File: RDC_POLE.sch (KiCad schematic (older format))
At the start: 32 parts, among them J1 CN_ARM, Q1 BC807, Q2 BC807, U2 AD8397ARZ, X1 8.192MHz

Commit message: agregado el segundo RDC, leds conectados a +5v, asignados footprints
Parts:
- removed C13: 100n, Capacitor_SMD:C_1206_3216Metric_Pad1.42x1.75mm_HandSolder, symbol Device:CP1
- removed R7: 10K, Resistor_SMD:R_1206_3216Metric_Pad1.42x1.75mm_HandSolder, symbol Device:R
- J1: value CN_ARM -> CN_POLE
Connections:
- net labels added: GPIO3
- net labels removed: GPIO2
- wire segments 129 -> 124

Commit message: cambios en el placement
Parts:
- renumbered AD1 to AD2, C11 to C14, C12 to C15, C14 to C16, C3 to C17, C6 to C18, C4 to C19, C7 to C20, C5 to C21, C8 to C22, C15 to C23, C9 to C24, C10 to C25, D1 to D3, D2 to D4, J1 to J2, Q1 to Q3, Q2 to Q4, R4 to R13, R6 to R14, R8 to R15, R9 to R16, R3 to R17, R1 to R18, R10 to R19, R11 to R20, R13 to R21, X1 to X2

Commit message: routeado completo, quedan 32 vias
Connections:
- wire segments 124 -> 126
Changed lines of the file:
@@
 Wire Wire Line
 	7900 4250 7600 4250
-Text Label 10400 4350 2    60   ~ 0
-COS
-Text Label 10400 4450 2    60   ~ 0
-COSLO
-Text Label 10400 4150 2    60   ~ 0
-SINLO
-Text Label 10400 4050 2    60   ~ 0
-SIN
-Wire Wire Line
-	10500 4450 10100 4450
-Wire Wire Line
-	10500 4350 10100 4350
-Wire Wire Line
-	10500 4150 10100 4150
-Wire Wire Line
-	10500 4050 10100 4050
-Text Label 10400 4550 2    60   ~ 0
+Text Label 10500 4050 2    60   ~ 0
 AGND
-Text Label 10400 4250 2    60   ~ 0
+Text Label 10500 3750 2    60   ~ 0
 AGND
-Text Label 10400 3950 2    60   ~ 0
+Text Label 10500 3450 2    60   ~ 0
 AGND
-Wire Wire Line
-	10500 4550 10100 4550
-Wire Wire Line
-	10500 4250 10100 4250
-Wire Wire Line
-	10500 3950 10100 3950
-Wire Wire Line
-	9950 3850 10500 3850
-Wire Wire Line
-	9950 3750 10500 3750
-$Comp
-L Connector:Screw_Terminal_01x09 J?
-U 1 1 5F08F1F4
-P 10700 4150
-AR Path="/5F08F1F4" Ref="J?"  Part="1"
-AR Path="/5EF45E27/5F08F1F4" Ref="J?"  Part="1"
-AR Path="/5F077C82/5F08F1F4" Ref="J2"  Part="1"
-F 0 "J2" H 10780 4192 50  0000 L CNN
-F 1 "CN_POLE" H 10780 4101 50  0000 L CNN
-F 2 "TerminalBlock_Phoenix:TerminalBlock_Phoenix_MKDS-1,5-9-5.08_1x09_P5.08mm_Horizontal" H 10700 4150 50  0001 C CNN
-F 3 "~" H 10700 4150 50  0001 C CNN
-	1    10700 4150
-	1    0    0    -1
-$EndComp
 $Comp
 L power:+12V #PWR?
@@
 	8300 4250 8300 5450
 Wire Wire Line
-	9950 3850 9950 5100
-Wire Wire Line
 	9500 5100 9300 5100
 Wire Wire Line
@@
 Wire Wire Line
 	9950 5100 9950 5450
-Wire Wire Line
-	9950 2950 9950 3300
 Wire Wire Line
 	9300 3300 9500 3300
@@
 Wire Wire Line
 	5800 2900 5800 2950
+Text Label 10500 3550 2    60   ~ 0
+SIN
+Text Label 10500 3650 2    60   ~ 0
+SINLO
+Wire Wire Line
+	9950 2950 9950 3300
+Text Label 10500 3250 2    60   ~ 0
+COS
+Text Label 10500 3350 2    60   ~ 0
+COSLO
+Wire Wire Line
+	9950 3850 9950 5100
+Wire Wire Line
+	10600 3250 10200 3250
+Wire Wire Line
+	10600 3350 10200 3350
+$Comp
+L Connector:Screw_Terminal_01x09 J?
+U 1 1 5F08F1F4
+P 10800 3650
+AR Path="/5F08F1F4" Ref="J?"  Part="1"
+AR Path="/5EF45E27/5F08F1F4" Ref="J?"  Part="1"
+AR Path="/5F077C82/5F08F1F4" Ref="J2"  Part="1"
+F 0 "J2" H 10880 3692 50  0000 L CNN
+F 1 "CN_POLE" H 10880 3601 50  0000 L CNN
+F 2 "TerminalBlock_Phoenix:TerminalBlock_Phoenix_MKDS-1,5-9-5.08_1x09_P5.08mm_Horizontal" H 10800 3650 50  0001 C CNN
+F 3 "~" H 10800 3650 50  0001 C CNN
+	1    10800 3650
+	1    0    0    -1
+$EndComp
+Wire Wire Line
+	10600 3450 10200 3450
+Wire Wire Line
+	10600 3750 10200 3750
+Wire Wire Line
+	10600 4050 10200 4050
+Wire Wire Line
+	10600 3550 10200 3550
+Wire Wire Line
+	10600 3650 10200 3650
+Wire Wire Line
+	10050 3950 10600 3950
+Wire Wire Line
+	9950 3850 10600 3850
+Connection ~ 9950 3850
+Wire Wire Line
+	9950 3750 10050 3750
+Wire Wire Line
+	10050 3750 10050 3950
+Connection ~ 9950 3750
 $EndSCHEMATC

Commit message: cambiados conectores, agregado conversor 3,3->TTL drivers
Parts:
- removed J2: CN_POLE, TerminalBlock_Phoenix:TerminalBlock_Phoenix_MKDS-1,5-9-5.08_1x09_P5.08mm_Horizontal, symbol Connector:Screw_Terminal_01x09
- added J4: COS, Connector_JST:JST_EH_S3B-EH_1x03_P2.50mm_Horizontal, symbol Connector_Generic:Conn_01x03
- added J5: SIN, Connector_JST:JST_EH_S3B-EH_1x03_P2.50mm_Horizontal, symbol Connector_Generic:Conn_01x03
- added J6: EXC, Connector_JST:JST_EH_S3B-EH_1x03_P2.50mm_Horizontal, symbol Connector_Generic:Conn_01x03
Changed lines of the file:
@@
 $Descr A4 11693 8268
 encoding utf-8
-Sheet 4 5
+Sheet 4 6
 Title ""
 Date ""
@@
 Text Label 10500 4050 2    60   ~ 0
 AGND
-Text Label 10500 3750 2    60   ~ 0
+Text Label 10500 3600 2    60   ~ 0
 AGND
-Text Label 10500 3450 2    60   ~ 0
+Text Label 10500 3150 2    60   ~ 0
 AGND
 $Comp
@@
 Wire Wire Line
 	5800 2900 5800 2950
-Text Label 10500 3550 2    60   ~ 0
+Text Label 10500 3400 2    60   ~ 0
 SIN
-Text Label 10500 3650 2    60   ~ 0
+Text Label 10500 3500 2    60   ~ 0
 SINLO
 Wire Wire Line
 	9950 2950 9950 3300
-Text Label 10500 3250 2    60   ~ 0
+Text Label 10500 2950 2    60   ~ 0
 COS
-Text Label 10500 3350 2    60   ~ 0
+Text Label 10500 3050 2    60   ~ 0
 COSLO
 Wire Wire Line
 	9950 3850 9950 5100
 Wire Wire Line
-	10600 3250 10200 3250
-Wire Wire Line
-	10600 3350 10200 3350
-$Comp
-L Connector:Screw_Terminal_01x09 J?
-U 1 1 5F08F1F4
-P 10800 3650
-AR Path="/5F08F1F4" Ref="J?"  Part="1"
-AR Path="/5EF45E27/5F08F1F4" Ref="J?"  Part="1"
-AR Path="/5F077C82/5F08F1F4" Ref="J2"  Part="1"
-F 0 "J2" H 10880 3692 50  0000 L CNN
-F 1 "CN_POLE" H 10880 3601 50  0000 L CNN
-F 2 "TerminalBlock_Phoenix:TerminalBlock_Phoenix_MKDS-1,5-9-5.08_1x09_P5.08mm_Horizontal" H 10800 3650 50  0001 C CNN
-F 3 "~" H 10800 3650 50  0001 C CNN
-	1    10800 3650
-	1    0    0    -1
-$EndComp
-Wire Wire Line
-	10600 3450 10200 3450
-Wire Wire Line
-	10600 3750 10200 3750
+	10600 2950 10200 2950
+Wire Wire Line
+	10600 3050 10200 3050
+Wire Wire Line
+	10600 3150 10200 3150
+Wire Wire Line
+	10600 3600 10200 3600
 Wire Wire Line
 	10600 4050 10200 4050
 Wire Wire Line
-	10600 3550 10200 3550
-Wire Wire Line
-	10600 3650 10200 3650
+	10600 3400 10200 3400
+Wire Wire Line
+	10600 3500 10200 3500
 Wire Wire Line
 	10050 3950 10600 3950
@@
 	10050 3750 10050 3950
 Connection ~ 9950 3750
+$Comp
+L Connector_Generic:Conn_01x03 J4
+U 1 1 5F0C4501
+P 10800 3050
+F 0 "J4" H 10880 3092 50  0000 L CNN
+F 1 "COS" H 10880 3001 50  0000 L CNN
+F 2 "Connector_JST:JST_EH_S3B-EH_1x03_P2.50mm_Horizontal" H 10800 3050 50  0001 C CNN
+F 3 "~" H 10800 3050 50  0001 C CNN
+	1    10800 3050
+	1    0    0    -1
+$EndComp
+$Comp
+L Connector_Generic:Conn_01x03 J5
+U 1 1 5F0C48DE
+P 10800 3500
+F 0 "J5" H 10880 3542 50  0000 L CNN
+F 1 "SIN" H 10880 3451 50  0000 L CNN
+F 2 "Connector_JST:JST_EH_S3B-EH_1x03_P2.50mm_Horizontal" H 10800 3500 50  0001 C CNN
+F 3 "~" H 10800 3500 50  0001 C CNN
+	1    10800 3500
+	1    0    0    -1
+$EndComp
+$Comp
+L Connector_Generic:Conn_01x03 J6
+U 1 1 5F0C52DE
+P 10800 3950
+F 0 "J6" H 10880 3992 50  0000 L CNN
+F 1 "EXC" H 10880 3901 50  0000 L CNN
+F 2 "Connector_JST:JST_EH_S3B-EH_1x03_P2.50mm_Horizontal" H 10800 3950 50  0001 C CNN
+F 3 "~" H 10800 3950 50  0001 C CNN
+	1    10800 3950
+	1    0    0    -1
+$EndComp
 $EndSCHEMATC

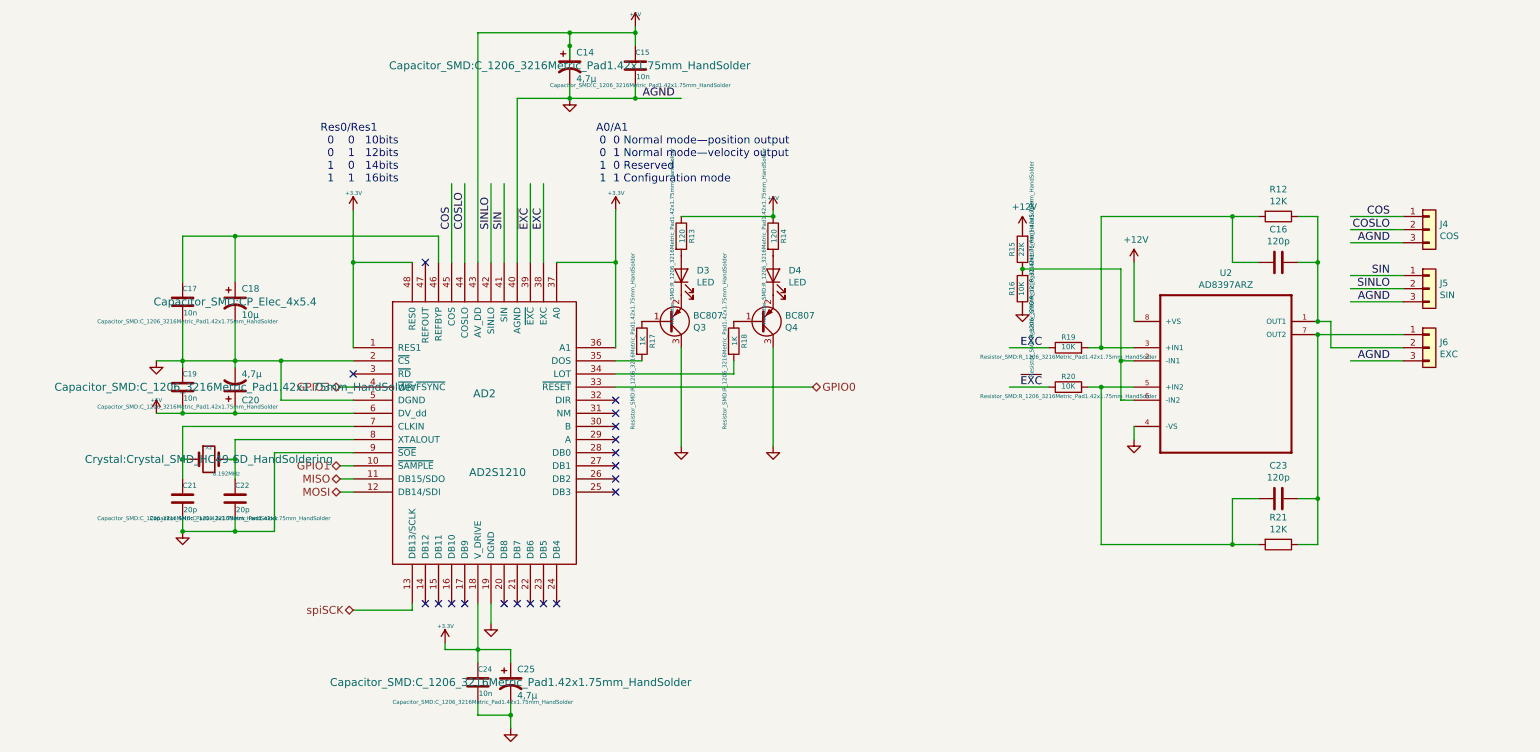
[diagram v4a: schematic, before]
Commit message: cambiado a conectores MOLEX KK, agregados test points para señales analogicas
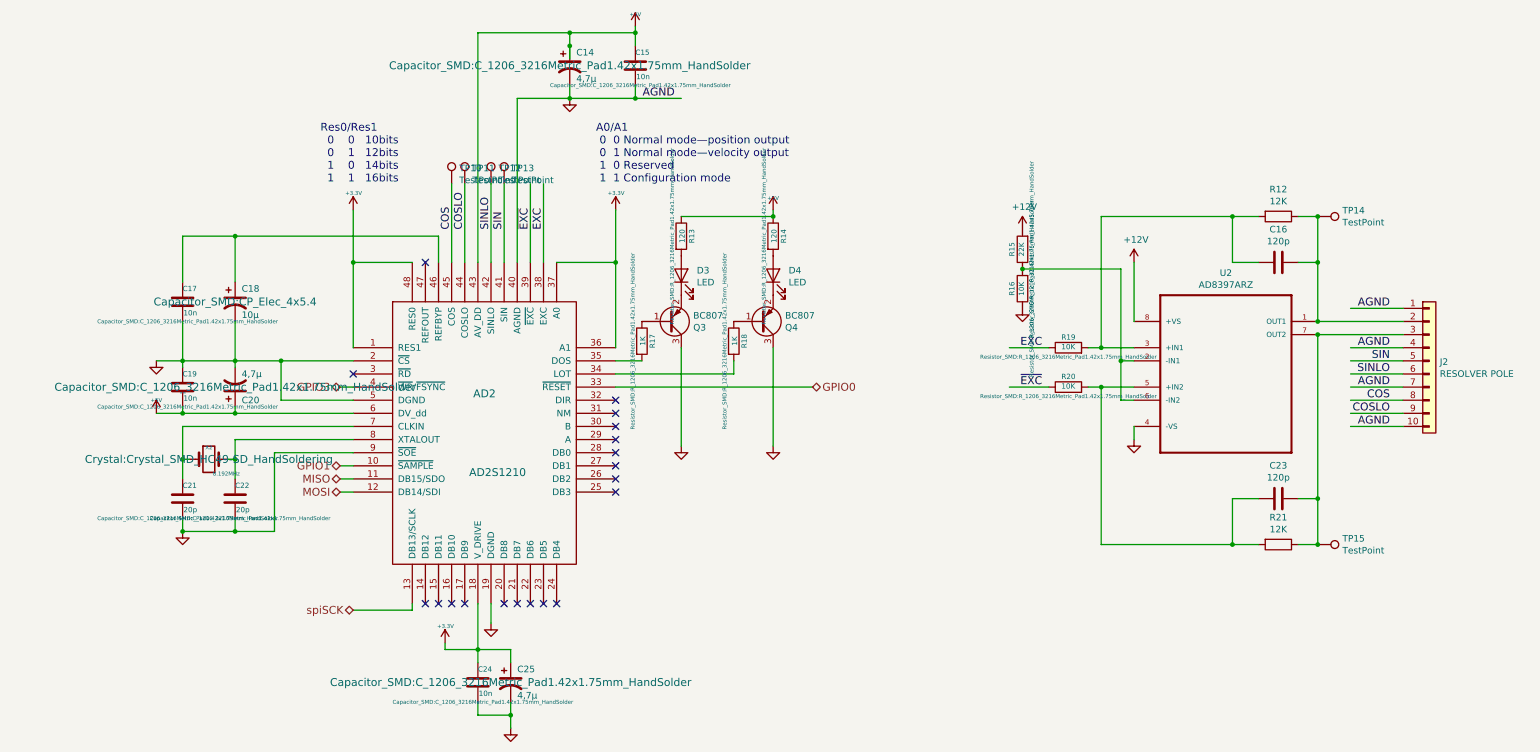
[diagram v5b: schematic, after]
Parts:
- removed J4: COS, Connector_JST:JST_EH_S3B-EH_1x03_P2.50mm_Horizontal, symbol Connector_Generic:Conn_01x03
- removed J5: SIN, Connector_JST:JST_EH_S3B-EH_1x03_P2.50mm_Horizontal, symbol Connector_Generic:Conn_01x03
- removed J6: EXC, Connector_JST:JST_EH_S3B-EH_1x03_P2.50mm_Horizontal, symbol Connector_Generic:Conn_01x03
- added J2: RESOLVER POLE, Connector_Molex:Molex_KK-254_AE-6410-10A_1x10_P2.54mm_Vertical, symbol Connector_Generic:Conn_01x10
- added TP10, TP11, TP12, TP13, TP14, TP15: TestPoint, TestPoint:TestPoint_THTPad_1.0x1.0mm_Drill0.5mm, symbol Connector:TestPoint
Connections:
- wire segments 126 -> 125
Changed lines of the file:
@@
 Wire Wire Line
 	7900 4250 7600 4250
-Text Label 10500 4050 2    60   ~ 0
+Text Label 10500 4550 2    60   ~ 0
 AGND
-Text Label 10500 3600 2    60   ~ 0
-AGND
-Text Label 10500 3150 2    60   ~ 0
+Text Label 10500 3950 2    60   ~ 0
 AGND
 $Comp
@@
 Wire Wire Line
 	5800 2900 5800 2950
-Text Label 10500 3400 2    60   ~ 0
-SIN
-Text Label 10500 3500 2    60   ~ 0
-SINLO
 Wire Wire Line
 	9950 2950 9950 3300
-Text Label 10500 2950 2    60   ~ 0
+Text Label 10500 4350 2    60   ~ 0
 COS
-Text Label 10500 3050 2    60   ~ 0
+Text Label 10500 4450 2    60   ~ 0
 COSLO
 Wire Wire Line
+	10600 4350 10200 4350
+Wire Wire Line
+	10600 4450 10200 4450
+Wire Wire Line
+	10600 3950 10200 3950
+Wire Wire Line
+	10600 4550 10200 4550
+Connection ~ 9950 3750
+$Comp
+L Connector_Generic:Conn_01x10 J2
+U 1 1 5F092EDC
+P 10800 4050
+F 0 "J2" H 10880 4042 50  0000 L CNN
+F 1 "RESOLVER POLE" H 10880 3951 50  0000 L CNN
+F 2 "Connector_Molex:Molex_KK-254_AE-6410-10A_1x10_P2.54mm_Vertical" H 10800 4050 50  0001 C CNN
+F 3 "~" H 10800 4050 50  0001 C CNN
+	1    10800 4050
+	1    0    0    -1
+$EndComp
+Text Label 10500 3650 2    60   ~ 0
+AGND
+Wire Wire Line
+	10600 3650 10200 3650
+$Comp
+L Connector:TestPoint TP14
+U 1 1 5F0B4618
+P 9950 2950
+F 0 "TP14" V 9904 3138 50  0000 L CNN
+F 1 "TestPoint" V 9995 3138 50  0000 L CNN
+F 2 "TestPoint:TestPoint_THTPad_1.0x1.0mm_Drill0.5mm" H 10150 2950 50  0001 C CNN
+F 3 "~" H 10150 2950 50  0001 C CNN
+	1    9950 2950
+	0    1    1    0
+$EndComp
+Connection ~ 9950 2950
+$Comp
+L Connector:TestPoint TP15
+U 1 1 5F0B53CC
+P 9950 5450
+F 0 "TP15" V 9904 5638 50  0000 L CNN
+F 1 "TestPoint" V 9995 5638 50  0000 L CNN
+F 2 "TestPoint:TestPoint_THTPad_1.0x1.0mm_Drill0.5mm" H 10150 5450 50  0001 C CNN
+F 3 "~" H 10150 5450 50  0001 C CNN
+	1    9950 5450
+	0    1    1    0
+$EndComp
+Connection ~ 9950 5450
+$Comp
+L Connector:TestPoint TP10
+U 1 1 5F0B5F68
+P 3350 2700
+F 0 "TP10" H 3408 2818 50  0000 L CNN
+F 1 "TestPoint" H 3408 2727 50  0000 L CNN
+F 2 "TestPoint:TestPoint_THTPad_1.0x1.0mm_Drill0.5mm" H 3550 2700 50  0001 C CNN
+F 3 "~" H 3550 2700 50  0001 C CNN
+	1    3350 2700
+	1    0    0    -1
+$EndComp
+$Comp
+L Connector:TestPoint TP11
+U 1 1 5F0B648D
+P 3450 2700
+F 0 "TP11" H 3508 2818 50  0000 L CNN
+F 1 "TestPoint" H 3508 2727 50  0000 L CNN
+F 2 "TestPoint:TestPoint_THTPad_1.0x1.0mm_Drill0.5mm" H 3650 2700 50  0001 C CNN
+F 3 "~" H 3650 2700 50  0001 C CNN
+	1    3450 2700
+	1    0    0    -1
+$EndComp
+$Comp
+L Connector:TestPoint TP12
+U 1 1 5F0B6AB2
+P 3650 2700
+F 0 "TP12" H 3708 2818 50  0000 L CNN
+F 1 "TestPoint" H 3708 2727 50  0000 L CNN
+F 2 "TestPoint:TestPoint_THTPad_1.0x1.0mm_Drill0.5mm" H 3850 2700 50  0001 C CNN
+F 3 "~" H 3850 2700 50  0001 C CNN
+	1    3650 2700
+	1    0    0    -1
+$EndComp
+$Comp
+L Connector:TestPoint TP13
+U 1 1 5F0B6E5F
+P 3750 2700
+F 0 "TP13" H 3808 2818 50  0000 L CNN
+F 1 "TestPoint" H 3808 2727 50  0000 L CNN
+F 2 "TestPoint:TestPoint_THTPad_1.0x1.0mm_Drill0.5mm" H 3950 2700 50  0001 C CNN
+F 3 "~" H 3950 2700 50  0001 C CNN
+	1    3750 2700
+	1    0    0    -1
+$EndComp
+Wire Wire Line
 	9950 3850 9950 5100
 Wire Wire Line
-	10600 2950 10200 2950
-Wire Wire Line
-	10600 3050 10200 3050
-Wire Wire Line
-	10600 3150 10200 3150
-Wire Wire Line
-	10600 3600 10200 3600
-Wire Wire Line
-	10600 4050 10200 4050
-Wire Wire Line
-	10600 3400 10200 3400
-Wire Wire Line
-	10600 3500 10200 3500
-Wire Wire Line
-	10050 3950 10600 3950
+	9950 3750 10600 3750
 Wire Wire Line
 	9950 3850 10600 3850
 Connection ~ 9950 3850
 Wire Wire Line
-	9950 3750 10050 3750
-Wire Wire Line
-	10050 3750 10050 3950
-Connection ~ 9950 3750
-$Comp
-L Connector_Generic:Conn_01x03 J4
-U 1 1 5F0C4501
-P 10800 3050
-F 0 "J4" H 10880 3092 50  0000 L CNN
-F 1 "COS" H 10880 3001 50  0000 L CNN
-F 2 "Connector_JST:JST_EH_S3B-EH_1x03_P2.50mm_Horizontal" H 10800 3050 50  0001 C CNN
-F 3 "~" H 10800 3050 50  0001 C CNN
-	1    10800 3050
-	1    0    0    -1
-$EndComp
-$Comp
-L Connector_Generic:Conn_01x03 J5
-U 1 1 5F0C48DE
-P 10800 3500
-F 0 "J5" H 10880 3542 50  0000 L CNN
-F 1 "SIN" H 10880 3451 50  0000 L CNN
-F 2 "Connector_JST:JST_EH_S3B-EH_1x03_P2.50mm_Horizontal" H 10800 3500 50  0001 C CNN
-F 3 "~" H 10800 3500 50  0001 C CNN
-	1    10800 3500
-	1    0    0    -1
-$EndComp
-$Comp
-L Connector_Generic:Conn_01x03 J6
-U 1 1 5F0C52DE
-P 10800 3950
-F 0 "J6" H 10880 3992 50  0000 L CNN
-F 1 "EXC" H 10880 3901 50  0000 L CNN
-F 2 "Connector_JST:JST_EH_S3B-EH_1x03_P2.50mm_Horizontal" H 10800 3950 50  0001 C CNN
-F 3 "~" H 10800 3950 50  0001 C CNN
-	1    10800 3950
-	1    0    0    -1
-$EndComp
+	10600 4150 10200 4150
+Wire Wire Line
+	10600 4050 10200 4050
+Wire Wire Line
+	10600 4250 10200 4250
+Text Label 10500 4150 2    60   ~ 0
+SINLO
+Text Label 10500 4050 2    60   ~ 0
+SIN
+Text Label 10500 4250 2    60   ~ 0
+AGND
 $EndSCHEMATC

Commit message: outline reducido, para revision por peers
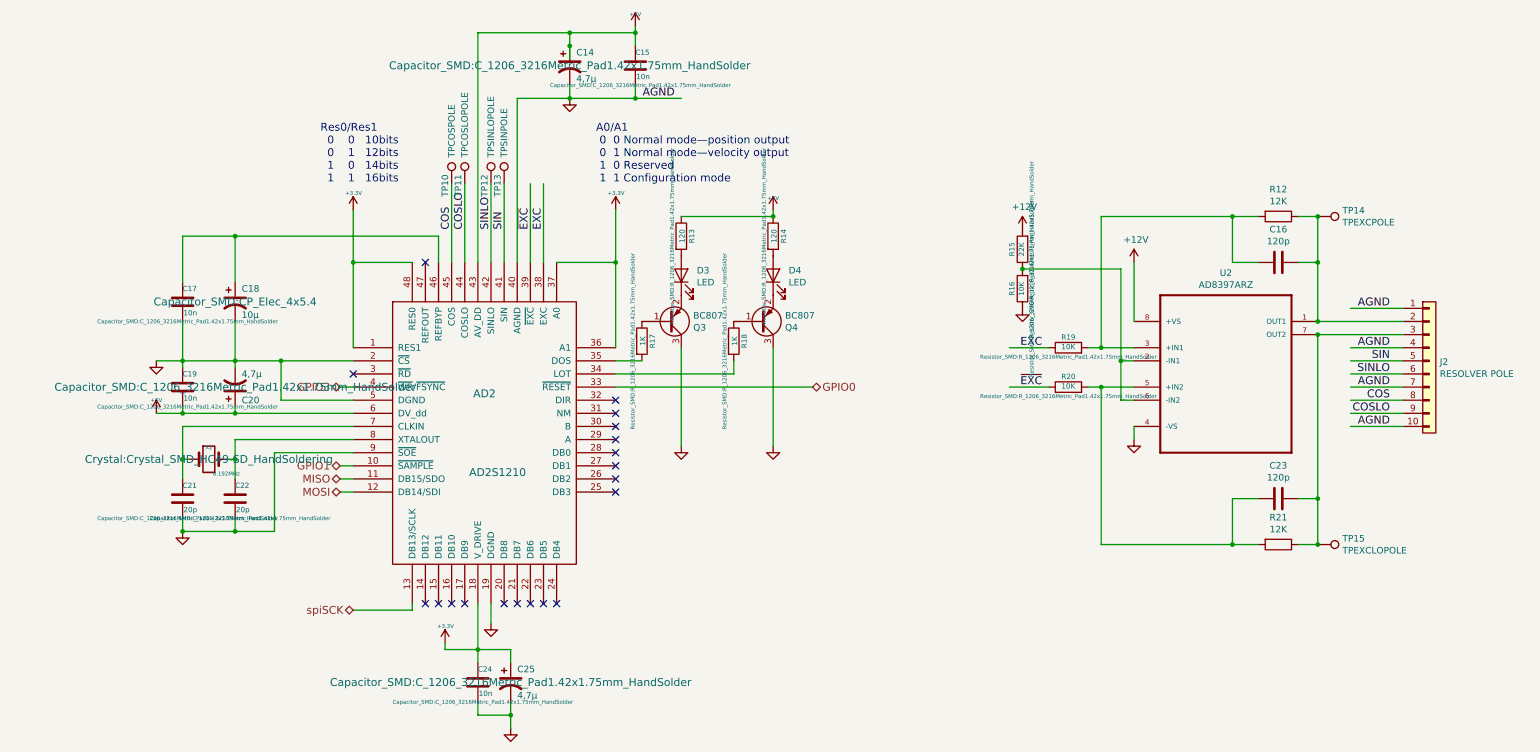
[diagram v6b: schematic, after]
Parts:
- TP10: value TestPoint -> TPCOSPOLE
- TP11: value TestPoint -> TPCOSLOPOLE
- TP12: value TestPoint -> TPSINLOPOLE
- TP13: value TestPoint -> TPSINPOLE
- TP14: value TestPoint -> TPEXCPOLE
- TP15: value TestPoint -> TPEXCLOPOLE
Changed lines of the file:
@@
 P 9950 2950
 F 0 "TP14" V 9904 3138 50  0000 L CNN
-F 1 "TestPoint" V 9995 3138 50  0000 L CNN
+F 1 "TPEXCPOLE" V 9995 3138 50  0000 L CNN
 F 2 "TestPoint:TestPoint_THTPad_1.0x1.0mm_Drill0.5mm" H 10150 2950 50  0001 C CNN
 F 3 "~" H 10150 2950 50  0001 C CNN
@@
 P 9950 5450
 F 0 "TP15" V 9904 5638 50  0000 L CNN
-F 1 "TestPoint" V 9995 5638 50  0000 L CNN
+F 1 "TPEXCLOPOLE" V 9995 5638 50  0000 L CNN
 F 2 "TestPoint:TestPoint_THTPad_1.0x1.0mm_Drill0.5mm" H 10150 5450 50  0001 C CNN
 F 3 "~" H 10150 5450 50  0001 C CNN
@@
 U 1 1 5F0B5F68
 P 3350 2700
-F 0 "TP10" H 3408 2818 50  0000 L CNN
-F 1 "TestPoint" H 3408 2727 50  0000 L CNN
+F 0 "TP10" V 3300 2600 50  0000 L CNN
+F 1 "TPCOSPOLE" V 3350 2900 50  0000 L CNN
 F 2 "TestPoint:TestPoint_THTPad_1.0x1.0mm_Drill0.5mm" H 3550 2700 50  0001 C CNN
 F 3 "~" H 3550 2700 50  0001 C CNN
@@
 U 1 1 5F0B648D
 P 3450 2700
-F 0 "TP11" H 3508 2818 50  0000 L CNN
-F 1 "TestPoint" H 3508 2727 50  0000 L CNN
+F 0 "TP11" V 3400 2600 50  0000 L CNN
+F 1 "TPCOSLOPOLE" V 3450 2900 50  0000 L CNN
 F 2 "TestPoint:TestPoint_THTPad_1.0x1.0mm_Drill0.5mm" H 3650 2700 50  0001 C CNN
 F 3 "~" H 3650 2700 50  0001 C CNN
@@
 U 1 1 5F0B6AB2
 P 3650 2700
-F 0 "TP12" H 3708 2818 50  0000 L CNN
-F 1 "TestPoint" H 3708 2727 50  0000 L CNN
+F 0 "TP12" V 3600 2600 50  0000 L CNN
+F 1 "TPSINLOPOLE" V 3650 2900 50  0000 L CNN
 F 2 "TestPoint:TestPoint_THTPad_1.0x1.0mm_Drill0.5mm" H 3850 2700 50  0001 C CNN
 F 3 "~" H 3850 2700 50  0001 C CNN
@@
 U 1 1 5F0B6E5F
 P 3750 2700
-F 0 "TP13" H 3808 2818 50  0000 L CNN
-F 1 "TestPoint" H 3808 2727 50  0000 L CNN
+F 0 "TP13" V 3700 2600 50  0000 L CNN
+F 1 "TPSINPOLE" V 3750 2900 50  0000 L CNN
 F 2 "TestPoint:TestPoint_THTPad_1.0x1.0mm_Drill0.5mm" H 3950 2700 50  0001 C CNN
 F 3 "~" H 3950 2700 50  0001 C CNN
